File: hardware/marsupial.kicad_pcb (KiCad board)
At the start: 4 copper layers, 53.1 x 98 mm, 207 parts, among them J101 DC IN, J102 DC OUT, J103 FPC, J201 USB_C_Receptacle_USB2.0, J301 MANUAL, J401 TagConnect, J501 MANUAL, J601 USB_C_Receptacle_USB2.0, J701 USB_C_Receptacle_USB2.0, Q201 DMP3028, Q202 DMP3028, Q203 DMP3028, Q204 MMBT3904, Q205 MMBT3904, Q206 DMP3028, Q207 MMBT3904, Q401 AO3400A, Q402 AO3400A, Q601 DMP3028, Q602 DMP3028, Q603 DMP3028, Q604 MMBT3904, Q605 MMBT3904, Q606 DMP3028, Q607 MMBT3904, SW1 RESET, U101 HT7550-1, U102 XC6206, U201 SRV05-4, U202 INA381A2IDSGR, U203 BL1551B, U301 SiC437, U401 STM32G071RBTx, U501 SiC437, U601 SRV05-4, U602 INA381A2IDSGR, U603 BL1551B, U701 USB2412-DZK-TR, Y401 12MHz, Y701 24MHz

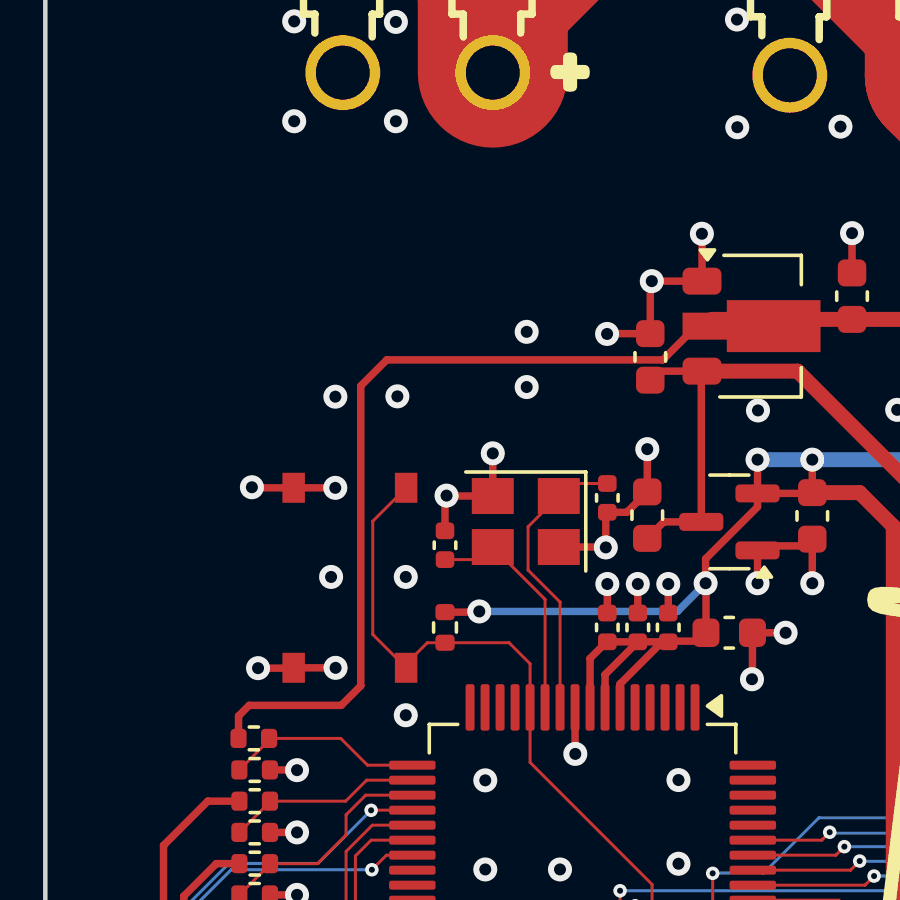
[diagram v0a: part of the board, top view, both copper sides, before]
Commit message: fix silkscreen
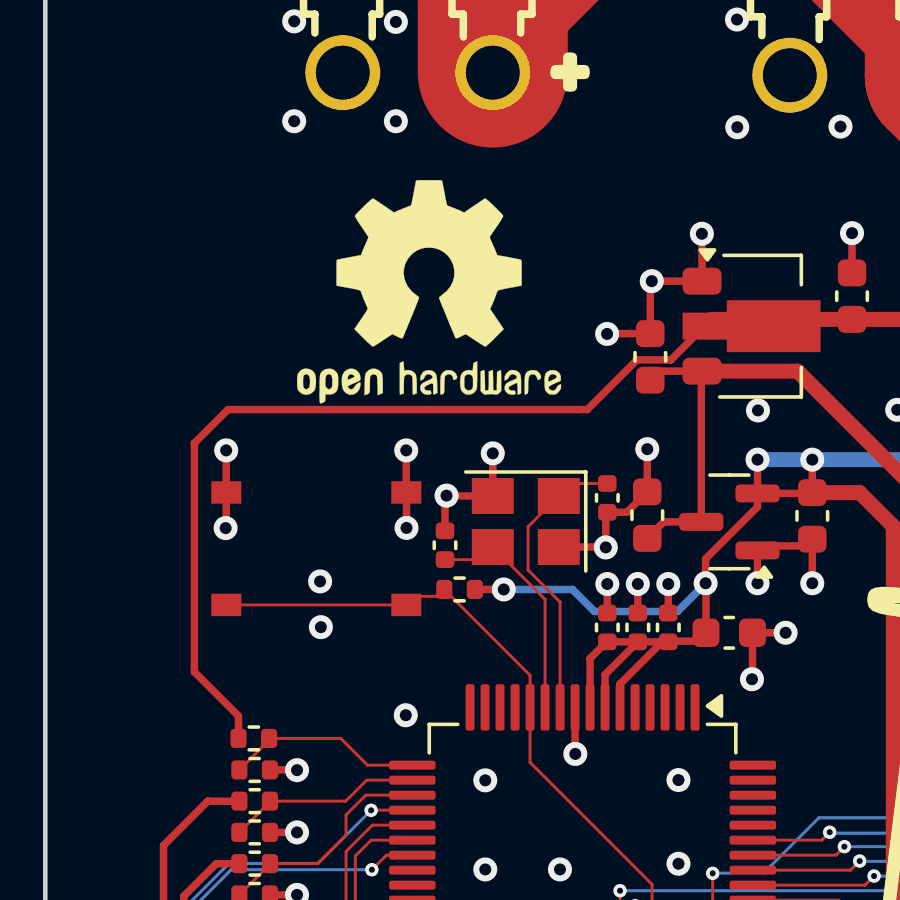
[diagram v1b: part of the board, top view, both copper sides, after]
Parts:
- added REF**: OSHW-Logo2_9.8x8mm_SilkScreen, Symbol:OSHW-Logo2_9.8x8mm_SilkScreen, F.Cu at (123.9, 68.0)
- moved SW1 1.48 mm to (120.2, 76.6), turned to 0 degrees
- moved R407 1.36 mm to (124.9, 77.9), turned to 180 degrees
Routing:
- net +24V: track 171.0 -> 172.5 mm
- net +3V3: track 222.1 -> 221.4 mm
- net /MCU/~{RST}: track 34.9 -> 34.2 mm
- net GND: track 178.2 -> 178.0 mm, vias 142 -> 138
